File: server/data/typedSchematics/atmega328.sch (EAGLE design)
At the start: 7 parts, among them U3 ATMEGA328, Y1 8MHz

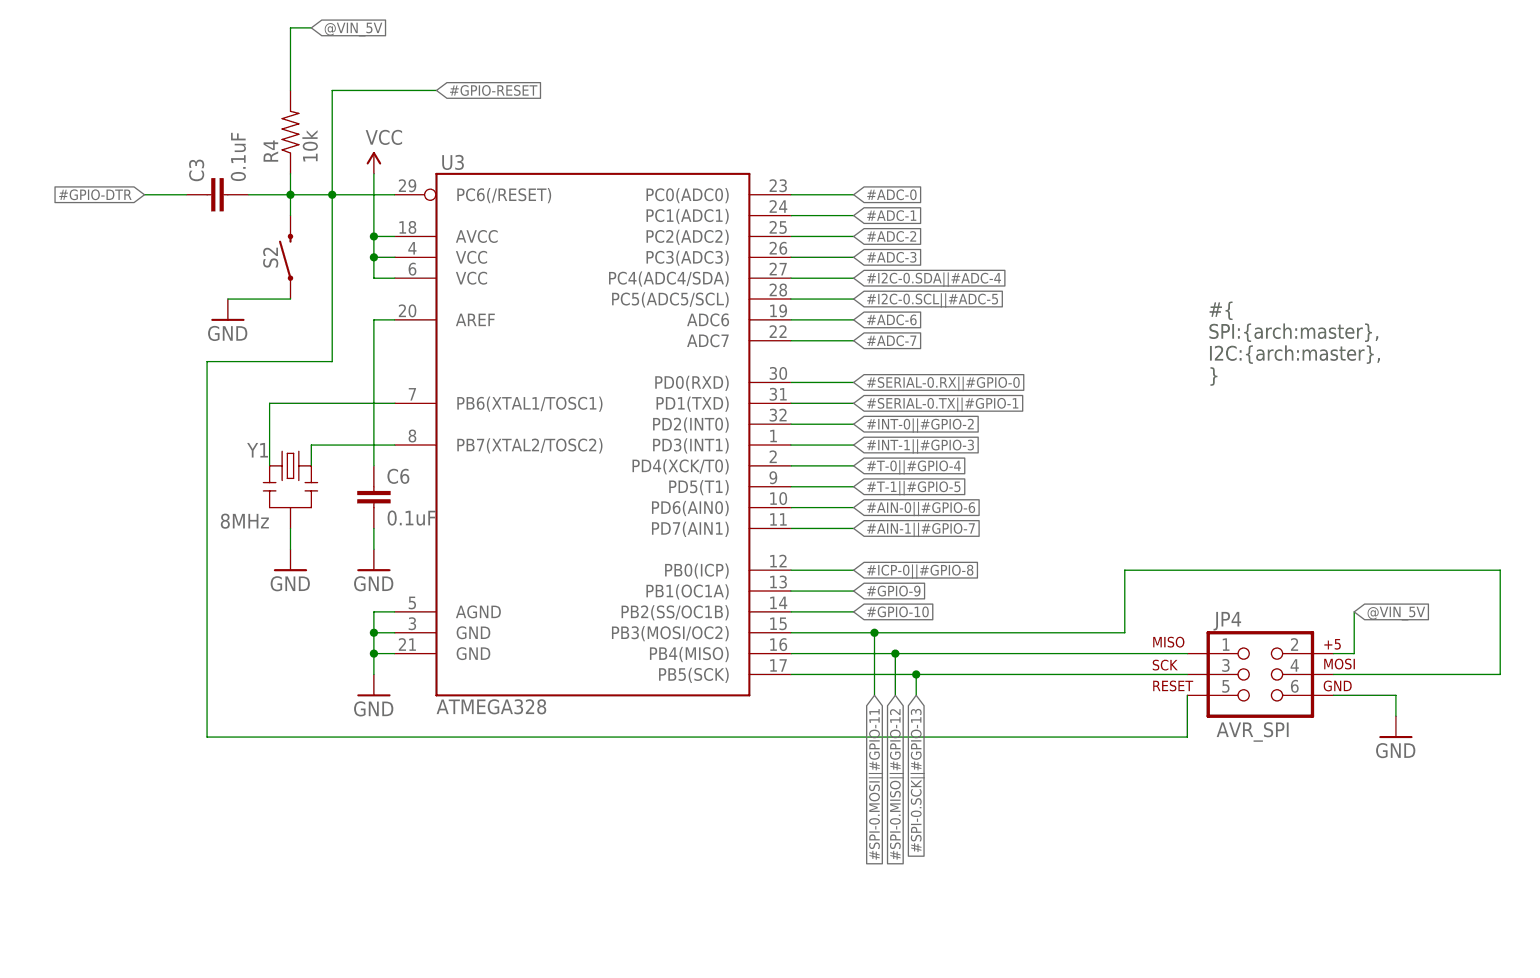
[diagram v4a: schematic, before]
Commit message: Adding I2C options in schematic + Voltage fix
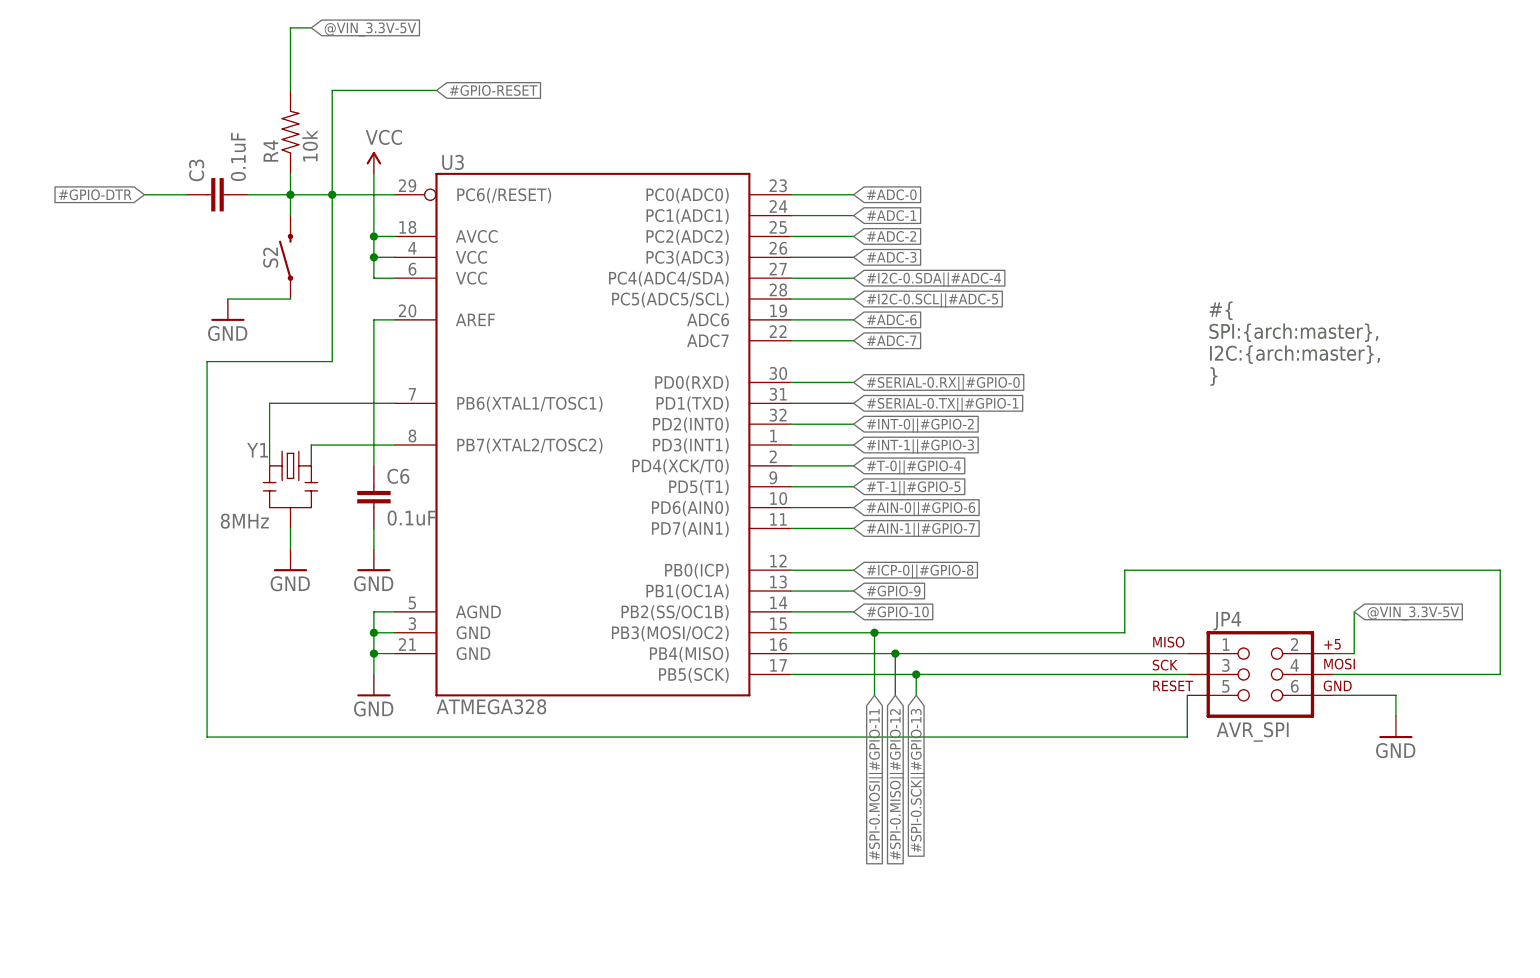
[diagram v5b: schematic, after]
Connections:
- net @VIN_5V renamed @VIN_3.3V-5V
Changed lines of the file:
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@@
 </segment>
 </net>
-<net name="@VIN_5V" class="0">
+<net name="@VIN_3.3V-5V" class="0">
 <segment>
 <pinref part="R4" gate="G$1" pin="2"/>

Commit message: Adding required annotation symbol
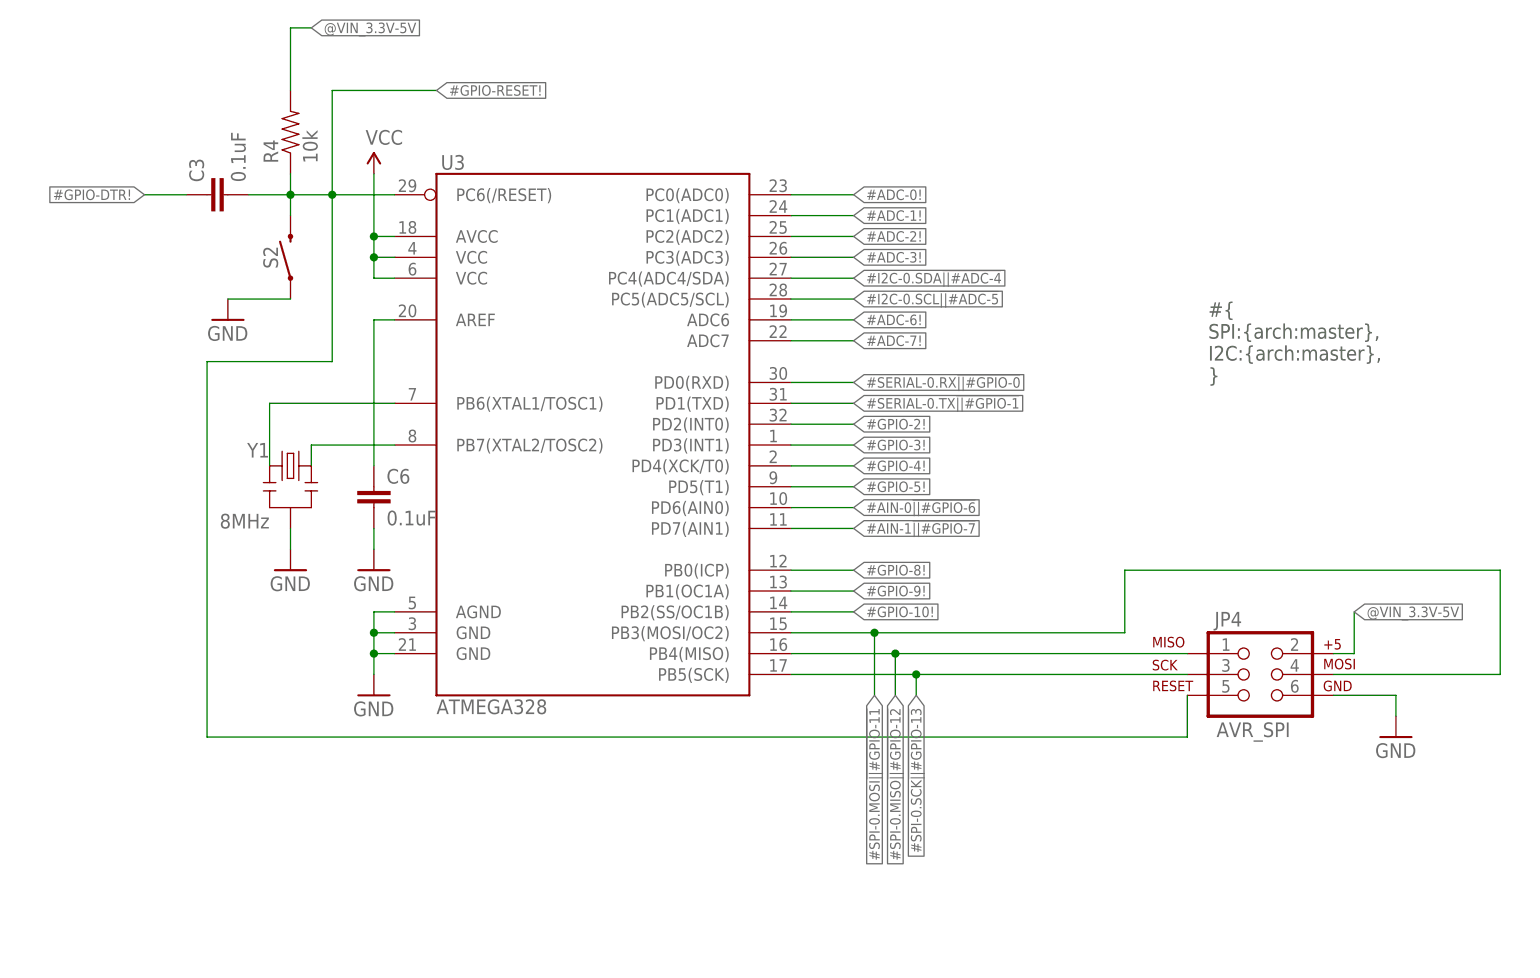
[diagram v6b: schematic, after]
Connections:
- net #ADC-0 renamed #ADC-0!
- net #ADC-1 renamed #ADC-1!
- net #ADC-2 renamed #ADC-2!
- net #ADC-3 renamed #ADC-3!
- net #ADC-6 renamed #ADC-6!
- net #ADC-7 renamed #ADC-7!
- net #AIN-0||#GPIO-6 renamed #AIN-0!||#GPIO-6!
- net #AIN-1||#GPIO-7 renamed #AIN-1!||#GPIO-7!
- net #GPIO-10 renamed #GPIO-10!
- net #GPIO-9 renamed #GPIO-9!
- net #GPIO-DTR renamed #GPIO-DTR!
- net #GPIO-RESET renamed #GPIO-RESET!
- net #I2C-0.SCL||#ADC-5 renamed #I2C-0.SCL!||#ADC-5!
- net #I2C-0.SDA||#ADC-4 renamed #I2C-0.SDA!||#ADC-4!
- net #ICP-0||#GPIO-8 renamed #GPIO-8!
- net #INT-0||#GPIO-2 renamed #GPIO-2!
- net #INT-1||#GPIO-3 renamed #GPIO-3!
- net #SERIAL-0.RX||#GPIO-0 renamed #SERIAL-0.RX!||#GPIO-0!
- net #SERIAL-0.TX||#GPIO-1 renamed #SERIAL-0.TX!||#GPIO-1!
- net #SPI-0.MISO||#GPIO-12 renamed #SPI-0.MISO!||#GPIO-12!
- net #SPI-0.MOSI||#GPIO-11 renamed #SPI-0.MOSI!||#GPIO-11!
- net #SPI-0.SCK||#GPIO-13 renamed #SPI-0.SCK!||#GPIO-13!
- net #T-0||#GPIO-4 renamed #GPIO-4!
- net #T-1||#GPIO-5 renamed #GPIO-5!
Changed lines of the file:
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@@
 </segment>
 </net>
-<net name="#GPIO-RESET" class="0">
+<net name="#GPIO-RESET!" class="0">
 <segment>
 <wire x1="63.5" y1="127" x2="63.5" y2="124.46" width="0.1524" layer="91"/>
@@
 </segment>
 </net>
-<net name="#GPIO-DTR" class="0">
+<net name="#GPIO-DTR!" class="0">
 <segment>
 <wire x1="50.8" y1="124.46" x2="45.72" y2="124.46" width="0.1524" layer="91"/>
@@
 </segment>
 </net>
-<net name="#ADC-0" class="0">
+<net name="#ADC-0!" class="0">
 <segment>
 <pinref part="U3" gate="G$1" pin="PC0(ADC0)"/>
@@
 </segment>
 </net>
-<net name="#ADC-1" class="0">
+<net name="#ADC-1!" class="0">
 <segment>
 <pinref part="U3" gate="G$1" pin="PC1(ADC1)"/>
@@
 </segment>
 </net>
-<net name="#ADC-2" class="0">
+<net name="#ADC-2!" class="0">
 <segment>
 <pinref part="U3" gate="G$1" pin="PC2(ADC2)"/>
@@
 </segment>
 </net>
-<net name="#ADC-3" class="0">
+<net name="#ADC-3!" class="0">
 <segment>
 <pinref part="U3" gate="G$1" pin="PC3(ADC3)"/>
@@
 </segment>
 </net>
-<net name="#I2C-0.SDA||#ADC-4" class="0">
+<net name="#I2C-0.SDA!||#ADC-4!" class="0">
 <segment>
 <pinref part="U3" gate="G$1" pin="PC4(ADC4/SDA)"/>
@@
 </segment>
 </net>
-<net name="#I2C-0.SCL||#ADC-5" class="0">
+<net name="#I2C-0.SCL!||#ADC-5!" class="0">
 <segment>
 <pinref part="U3" gate="G$1" pin="PC5(ADC5/SCL)"/>
@@
 </segment>
 </net>
-<net name="#ADC-6" class="0">
+<net name="#ADC-6!" class="0">
 <segment>
 <pinref part="U3" gate="G$1" pin="ADC6"/>
@@
 </segment>
 </net>
-<net name="#ADC-7" class="0">
+<net name="#ADC-7!" class="0">
 <segment>
 <pinref part="U3" gate="G$1" pin="ADC7"/>
@@
 </segment>
 </net>
-<net name="#SPI-0.MOSI||#GPIO-11" class="0">
+<net name="#SPI-0.MOSI!||#GPIO-11!" class="0">
 <segment>
 <pinref part="JP4" gate="G$1" pin="4"/>
@@
 </segment>
 </net>
-<net name="#SPI-0.MISO||#GPIO-12" class="0">
+<net name="#SPI-0.MISO!||#GPIO-12!" class="0">
 <segment>
 <pinref part="U3" gate="G$1" pin="PB4(MISO)"/>
@@
 </segment>
 </net>
-<net name="#SPI-0.SCK||#GPIO-13" class="0">
+<net name="#SPI-0.SCK!||#GPIO-13!" class="0">
 <segment>
 <pinref part="JP4" gate="G$1" pin="3"/>
@@
 </segment>
 </net>
-<net name="#SERIAL-0.RX||#GPIO-0" class="0">
+<net name="#SERIAL-0.RX!||#GPIO-0!" class="0">
 <segment>
 <pinref part="U3" gate="G$1" pin="PD0(RXD)"/>
@@
 </segment>
 </net>
-<net name="#SERIAL-0.TX||#GPIO-1" class="0">
+<net name="#SERIAL-0.TX!||#GPIO-1!" class="0">
 <segment>
 <pinref part="U3" gate="G$1" pin="PD1(TXD)"/>
@@
 </segment>
 </net>
-<net name="#INT-0||#GPIO-2" class="0">
+<net name="#GPIO-2!" class="0">
 <segment>
 <pinref part="U3" gate="G$1" pin="PD2(INT0)"/>
@@
 </segment>
 </net>
-<net name="#INT-1||#GPIO-3" class="0">
+<net name="#GPIO-3!" class="0">
 <segment>
 <pinref part="U3" gate="G$1" pin="PD3(INT1)"/>
@@
 </segment>
 </net>
-<net name="#T-0||#GPIO-4" class="0">
+<net name="#GPIO-4!" class="0">
 <segment>
 <pinref part="U3" gate="G$1" pin="PD4(XCK/T0)"/>
@@
 </segment>
 </net>
-<net name="#T-1||#GPIO-5" class="0">
+<net name="#GPIO-5!" class="0">
 <segment>
 <pinref part="U3" gate="G$1" pin="PD5(T1)"/>
@@
 </segment>
 </net>
-<net name="#AIN-0||#GPIO-6" class="0">
+<net name="#AIN-0!||#GPIO-6!" class="0">
 <segment>
 <pinref part="U3" gate="G$1" pin="PD6(AIN0)"/>
@@
 </segment>
 </net>
-<net name="#AIN-1||#GPIO-7" class="0">
+<net name="#AIN-1!||#GPIO-7!" class="0">
 <segment>
 <pinref part="U3" gate="G$1" pin="PD7(AIN1)"/>
@@
 </segment>
 </net>
-<net name="#ICP-0||#GPIO-8" class="0">
+<net name="#GPIO-8!" class="0">
 <segment>
 <pinref part="U3" gate="G$1" pin="PB0(ICP)"/>
@@
 </segment>
 </net>
-<net name="#GPIO-9" class="0">
+<net name="#GPIO-9!" class="0">
 <segment>
 <pinref part="U3" gate="G$1" pin="PB1(OC1A)"/>
@@
 </segment>
 </net>
-<net name="#GPIO-10" class="0">
+<net name="#GPIO-10!" class="0">
 <segment>
 <pinref part="U3" gate="G$1" pin="PB2(SS/OC1B)"/>

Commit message: Update server side schematics
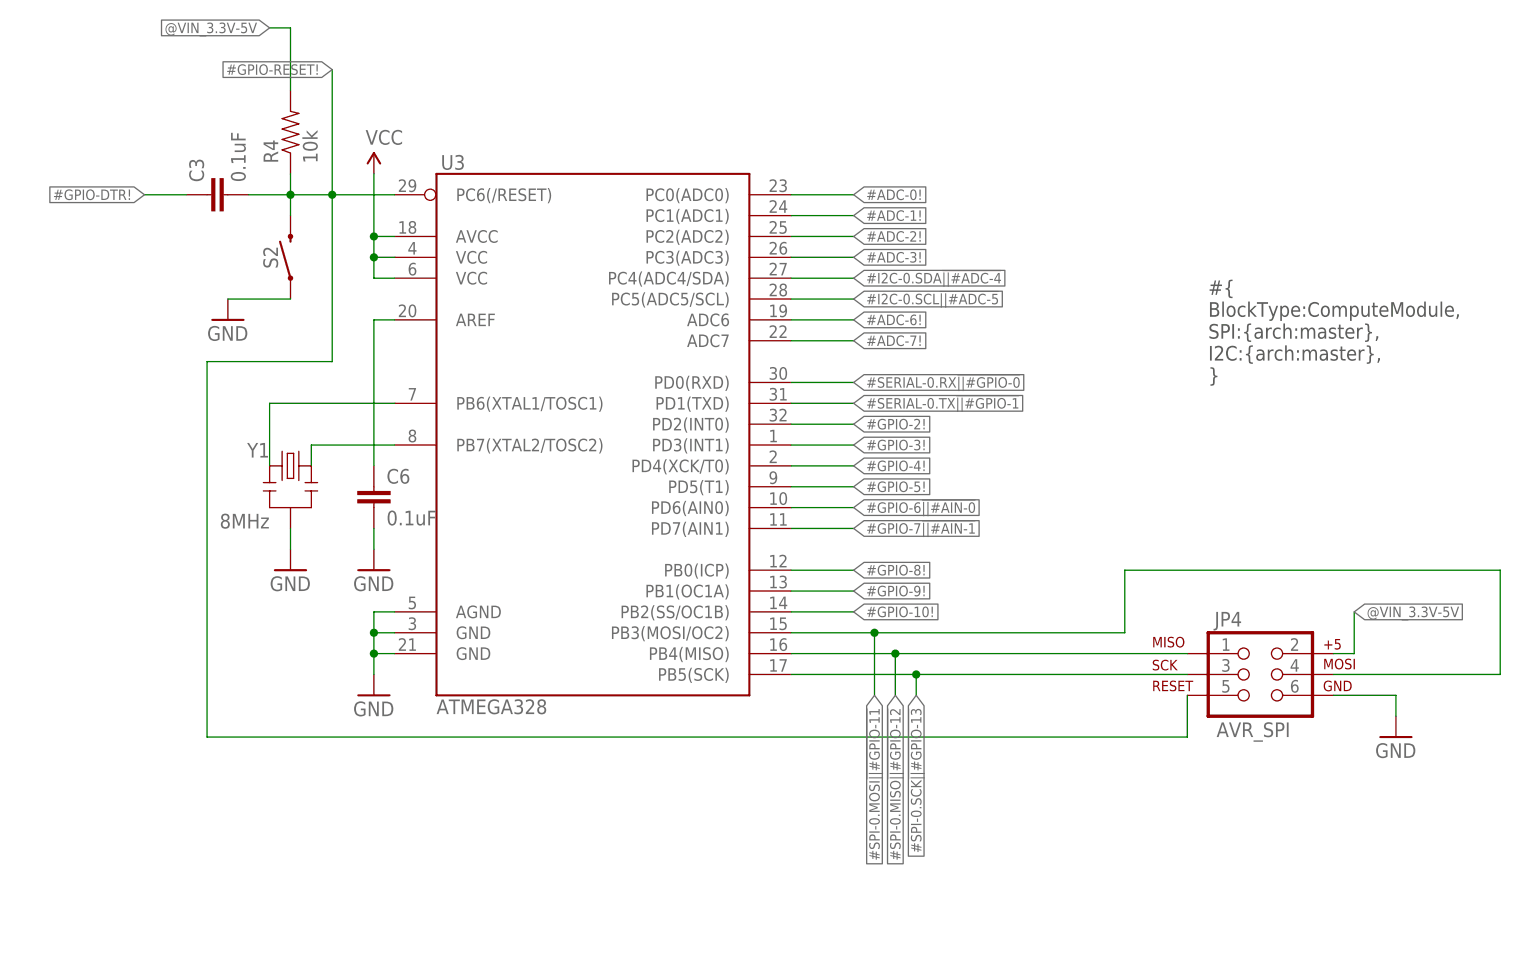
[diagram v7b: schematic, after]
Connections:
- net #AIN-0!||#GPIO-6! renamed #GPIO-6!||#AIN-0!
- net #AIN-1!||#GPIO-7! renamed #GPIO-7!||#AIN-1!
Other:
- note added: "#{ BlockType:ComputeModule, SPI:{arch:master}, I2C:{arch:master}, }"
- note removed: "#{ SPI:{arch:master}, I2C:{arch:master}, }"
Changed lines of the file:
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@@
 <plain>
 <text x="175.26" y="101.6" size="1.778" layer="97">#{
+BlockType:ComputeModule,
 SPI:{arch:master},
 I2C:{arch:master},
@@
 <pinref part="S2" gate="G$1" pin="2"/>
 <junction x="68.58" y="124.46"/>
-<wire x1="68.58" y1="124.46" x2="68.58" y2="137.16" width="0.1524" layer="91"/>
-<wire x1="68.58" y1="137.16" x2="81.28" y2="137.16" width="0.1524" layer="91"/>
-<label x="81.28" y="137.16" size="1.27" layer="95" xref="yes"/>
+<wire x1="68.58" y1="124.46" x2="68.58" y2="139.7" width="0.1524" layer="91"/>
+<label x="68.58" y="139.7" size="1.27" layer="95" rot="R180" xref="yes"/>
 <pinref part="JP4" gate="G$1" pin="5"/>
 <wire x1="172.72" y1="63.5" x2="172.72" y2="58.42" width="0.1524" layer="91"/>
@@
 </segment>
 </net>
-<net name="#AIN-0!||#GPIO-6!" class="0">
+<net name="#GPIO-6!||#AIN-0!" class="0">
 <segment>
 <pinref part="U3" gate="G$1" pin="PD6(AIN0)"/>
@@
 </segment>
 </net>
-<net name="#AIN-1!||#GPIO-7!" class="0">
+<net name="#GPIO-7!||#AIN-1!" class="0">
 <segment>
 <pinref part="U3" gate="G$1" pin="PD7(AIN1)"/>
@@
 <pinref part="R4" gate="G$1" pin="2"/>
 <wire x1="63.5" y1="137.16" x2="63.5" y2="144.78" width="0.1524" layer="91"/>
-<wire x1="63.5" y1="144.78" x2="66.04" y2="144.78" width="0.1524" layer="91"/>
-<label x="66.04" y="144.78" size="1.27" layer="95" xref="yes"/>
-</segment>
-<segment>
+<wire x1="63.5" y1="144.78" x2="60.96" y2="144.78" width="0.1524" layer="91"/>
+<label x="60.96" y="144.78" size="1.27" layer="95" rot="R180" xref="yes"/>
+</segment>
+<segment>
